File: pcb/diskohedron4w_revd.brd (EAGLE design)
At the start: 87.2 x 55.5 mm, 64 parts

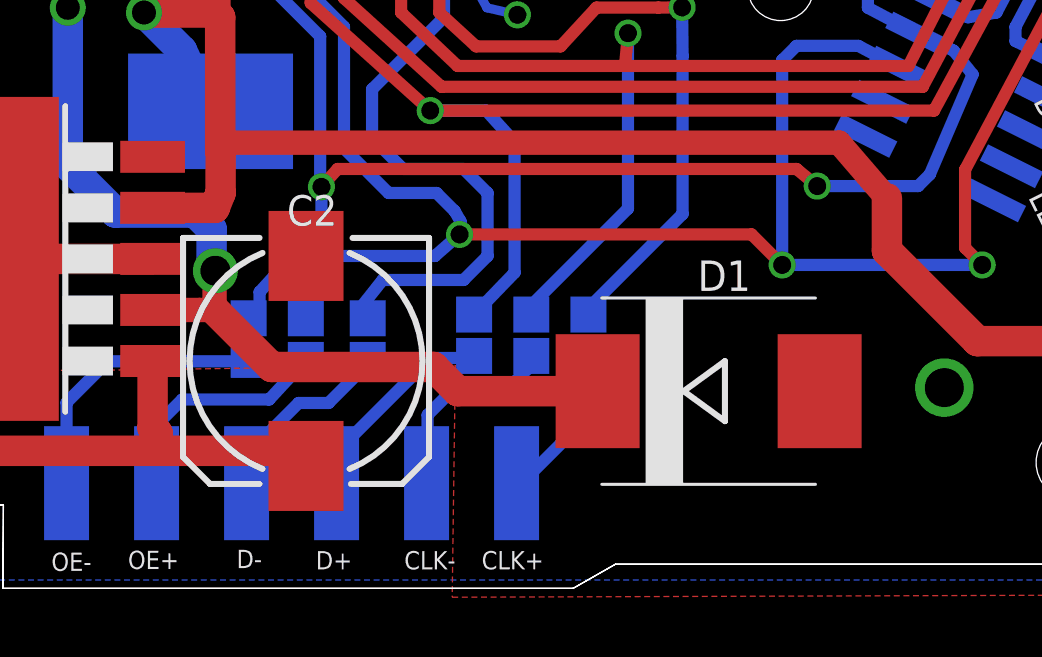
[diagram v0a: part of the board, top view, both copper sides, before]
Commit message: added stencil for rev.d
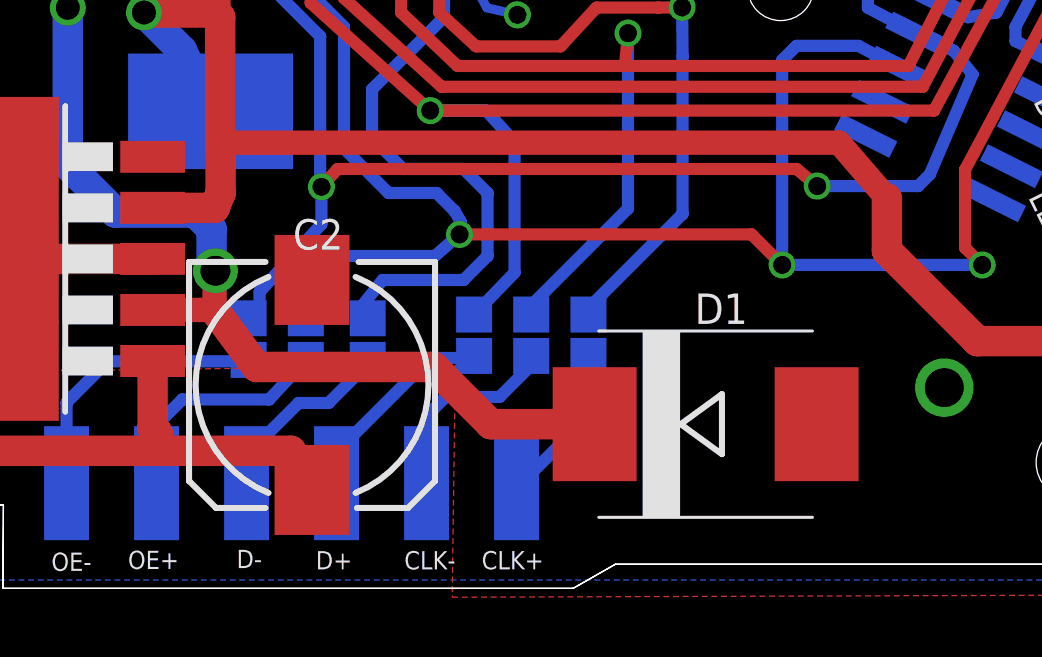
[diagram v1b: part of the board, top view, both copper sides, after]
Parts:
- moved D1 1.10 mm to (45.9, 4.69)
- moved C2 0.82 mm to (32.7, 6.00)
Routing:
- net IN+24V: track 27.0 -> 27.7 mm
- net N$2: track 41.0 -> 41.5 mm
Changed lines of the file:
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@@
 <layer number="20" name="Dimension" color="15" fill="1" visible="yes" active="yes"/>
 <layer number="21" name="tPlace" color="7" fill="1" visible="no" active="yes"/>
-<layer number="22" name="bPlace" color="7" fill="1" visible="yes" active="yes"/>
+<layer number="22" name="bPlace" color="7" fill="1" visible="no" active="yes"/>
 <layer number="23" name="tOrigins" color="15" fill="1" visible="no" active="yes"/>
-<layer number="24" name="bOrigins" color="15" fill="1" visible="yes" active="yes"/>
+<layer number="24" name="bOrigins" color="15" fill="1" visible="no" active="yes"/>
 <layer number="25" name="tNames" color="7" fill="1" visible="no" active="yes"/>
-<layer number="26" name="bNames" color="7" fill="1" visible="yes" active="yes"/>
+<layer number="26" name="bNames" color="7" fill="1" visible="no" active="yes"/>
 <layer number="27" name="tValues" color="7" fill="1" visible="no" active="yes"/>
-<layer number="28" name="bValues" color="7" fill="1" visible="yes" active="yes"/>
+<layer number="28" name="bValues" color="7" fill="1" visible="no" active="yes"/>
 <layer number="29" name="tStop" color="7" fill="3" visible="no" active="yes"/>
 <layer number="30" name="bStop" color="7" fill="6" visible="no" active="yes"/>
@@
 <layer number="113" name="guidesss" color="12" fill="1" visible="no" active="yes"/>
 <layer number="114" name="circles" color="12" fill="1" visible="no" active="yes"/>
-<layer number="115" name="bSilk" color="6" fill="1" visible="no" active="yes"/>
+<layer number="115" name="bSilk" color="6" fill="1" visible="yes" active="yes"/>
 <layer number="116" name="Patch_BOT" color="7" fill="1" visible="no" active="yes"/>
 <layer number="117" name="geo_hellper_Milling" color="11" fill="1" visible="no" active="yes"/>
@@
 <layer number="250" name="Descript" color="7" fill="1" visible="no" active="yes"/>
 <layer number="251" name="SMDround" color="7" fill="1" visible="no" active="yes"/>
-<layer number="253" name="geo_helper_axis" color="14" fill="1" visible="yes" active="yes"/>
+<layer number="253" name="geo_helper_axis" color="14" fill="1" visible="no" active="yes"/>
 <layer number="254" name="cooling" color="7" fill="1" visible="no" active="yes"/>
 <layer number="255" name="geo-helper" color="13" fill="1" visible="yes" active="yes"/>
@@
 <attribute name="NAME" x="73.34514375" y="50.135646875" size="1.27" layer="25" rot="R31.5"/>
 </element>
-<element name="C2" library="rcl" package="175TMP-0810" value="220uF" x="32.548465625" y="6.801421875" smashed="yes" rot="R270">
-<attribute name="NAME" x="31.913003125" y="11.31103125" size="1.016" layer="25"/>
+<element name="C2" library="rcl" package="175TMP-0810" value="220uF" x="32.748465625" y="6.001421875" smashed="yes" rot="R270">
+<attribute name="NAME" x="32.113003125" y="10.51103125" size="1.016" layer="25"/>
 </element>
 <element name="1D" library="diskohedron" package="SOT23-5" value="DS90LV011A" x="37.319575" y="20.958203125" smashed="yes" rot="MR333.4"/>
@@
 </element>
 <element name="L1" library="inductors" package="DR127" value="30uH" x="29.365028125" y="20.096415625" smashed="yes" rot="MR270"/>
-<element name="D1" library="eagle-ltspice" package="DIODE_SMC" value="1N5824 3A" x="45.96789375" y="5.793409375" smashed="yes">
-<attribute name="SPICEMODEL" value="diode" x="45.96789375" y="5.793409375" size="1.778" layer="27" display="off"/>
-<attribute name="SPICEPREFIX" value="D" x="45.96789375" y="5.793409375" size="1.778" layer="27" display="off"/>
-<attribute name="NAME" x="45.60389375" y="9.134909375" size="1.016" layer="25"/>
+<element name="D1" library="eagle-ltspice" package="DIODE_SMC" value="1N5824 3A" x="45.86789375" y="4.693409375" smashed="yes">
+<attribute name="SPICEMODEL" value="diode" x="45.86789375" y="4.693409375" size="1.778" layer="27" display="off"/>
+<attribute name="SPICEPREFIX" value="D" x="45.86789375" y="4.693409375" size="1.778" layer="27" display="off"/>
+<attribute name="NAME" x="45.50389375" y="8.034909375" size="1.016" layer="25"/>
 </element>
 <element name="JP1" library="SparkFun-Connectors" package="1X05" value="EXTBRD" x="63.4040375" y="19.644678125" smashed="yes" rot="R243"/>
@@
 <wire x1="29.4" y1="11.2" x2="29.4" y2="9.934165625" width="1.016" layer="16"/>
 <wire x1="29.4" y1="9.934165625" x2="29.5264375" y2="9.807728125" width="1.016" layer="16"/>
-<wire x1="42.26789375" y1="5.793409375" x2="37.606590625" y2="5.793409375" width="1.016" layer="1"/>
-<wire x1="37.606590625" y1="5.793409375" x2="36.8" y2="6.6" width="1.016" layer="1"/>
-<wire x1="36.8" y1="6.6" x2="31.4" y2="6.6" width="1.016" layer="1"/>
-<wire x1="31.4" y1="6.6" x2="29.5" y2="8.5" width="1.016" layer="1"/>
+<wire x1="42.16789375" y1="4.693409375" x2="38.706590625" y2="4.693409375" width="1.016" layer="1"/>
+<wire x1="38.706590625" y1="4.693409375" x2="36.8" y2="6.6" width="1.016" layer="1"/>
+<wire x1="36.8" y1="6.6" x2="30.9" y2="6.6" width="1.016" layer="1"/>
+<wire x1="30.9" y1="6.6" x2="29.5" y2="8.5" width="1.016" layer="1"/>
 </signal>
 <signal name="DATAOUT-L">
@@
 <contactref element="LM2586" pad="1"/>
 <wire x1="32.044859375" y1="3.805028125" x2="27.6" y2="3.805028125" width="1.016" layer="1"/>
-<wire x1="32.044859375" y1="3.805028125" x2="32.548465625" y2="3.301421875" width="1.016" layer="1"/>
+<wire x1="32.044859375" y1="3.805028125" x2="32.748465625" y2="2.501421875" width="1.016" layer="1"/>
 <wire x1="27.433446875" y1="6.798484375" x2="27.433446875" y2="4.566553125" width="1.016" layer="1"/>
 <wire x1="27.433446875" y1="4.566553125" x2="27.6" y2="4.4" width="1.016" layer="1"/>
